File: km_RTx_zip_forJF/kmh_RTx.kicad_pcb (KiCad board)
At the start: 2 copper layers, 50 x 40 mm, 33 parts, among them IC1 ADP7118AUJZ-3.3-R7, J1 DE9_Receptacle, J3 Conn_Coaxial, J4 M80-5420442, T1 ETC4-1-2TR, U1 AD4PS-1+, U2 BD80FD0WHFP-TR, X1 3QHTF53-17.734-OE, X2 ASE-25.000MHZ-L-C-T, X3 3QHTF53-35.430-OE, X4 ASE-50.000MHZ-L-C-T

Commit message: C:\Users\khernandez\KiCad\KiCad-Project
Preliminary Part Placement
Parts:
- removed J1: DE9_Receptacle, Connector_Dsub:DSUB-9_Female_Horizontal_P2.77x2.84mm_EdgePinOffset9.40mm
- removed J3: Conn_Coaxial, Connector_Coaxial:SMA_Amphenol_132291_Vertical
- removed J4: M80-5420442, Connector:M80-5420442
- added H10: 2111-2-00-44-00-00-07-0, Turrets:2111200440000070, F.Cu at (94.0, 42.0)
- added H11: 2111-2-00-44-00-00-07-0, Turrets:2111200440000070, F.Cu at (94.0, 45.0)
- added H12: 2111-2-00-44-00-00-07-0, Turrets:2111200440000070, F.Cu at (94.0, 48.0)
- added H13: 2111-2-00-44-00-00-07-0, Turrets:2111200440000070, F.Cu at (94.0, 51.0)
- added H14: 2111-2-00-44-00-00-07-0, Turrets:2111200440000070, F.Cu at (129.5, 35.5)
- added H15: 2111-2-00-44-00-00-07-0, Turrets:2111200440000070, F.Cu at (129.5, 38.5)
- added H16: 2111-2-00-44-00-00-07-0, Turrets:2111200440000070, F.Cu at (129.5, 50.0)
- added H5: 2111-2-00-44-00-00-07-0, Turrets:2111200440000070, F.Cu at (90.5, 40.0)
- added H6: 2111-2-00-44-00-00-07-0, Turrets:2111200440000070, F.Cu at (90.5, 43.0)
- added H7: 2111-2-00-44-00-00-07-0, Turrets:2111200440000070, F.Cu at (90.5, 46.0)
- added H8: 2111-2-00-44-00-00-07-0, Turrets:2111200440000070, F.Cu at (90.5, 49.0)
- added H9: 2111-2-00-44-00-00-07-0, Turrets:2111200440000070, F.Cu at (90.5, 52.0)
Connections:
- R3 pad 2: Net-(J4-Pad3) -> unconnected-(R3-Pad2)

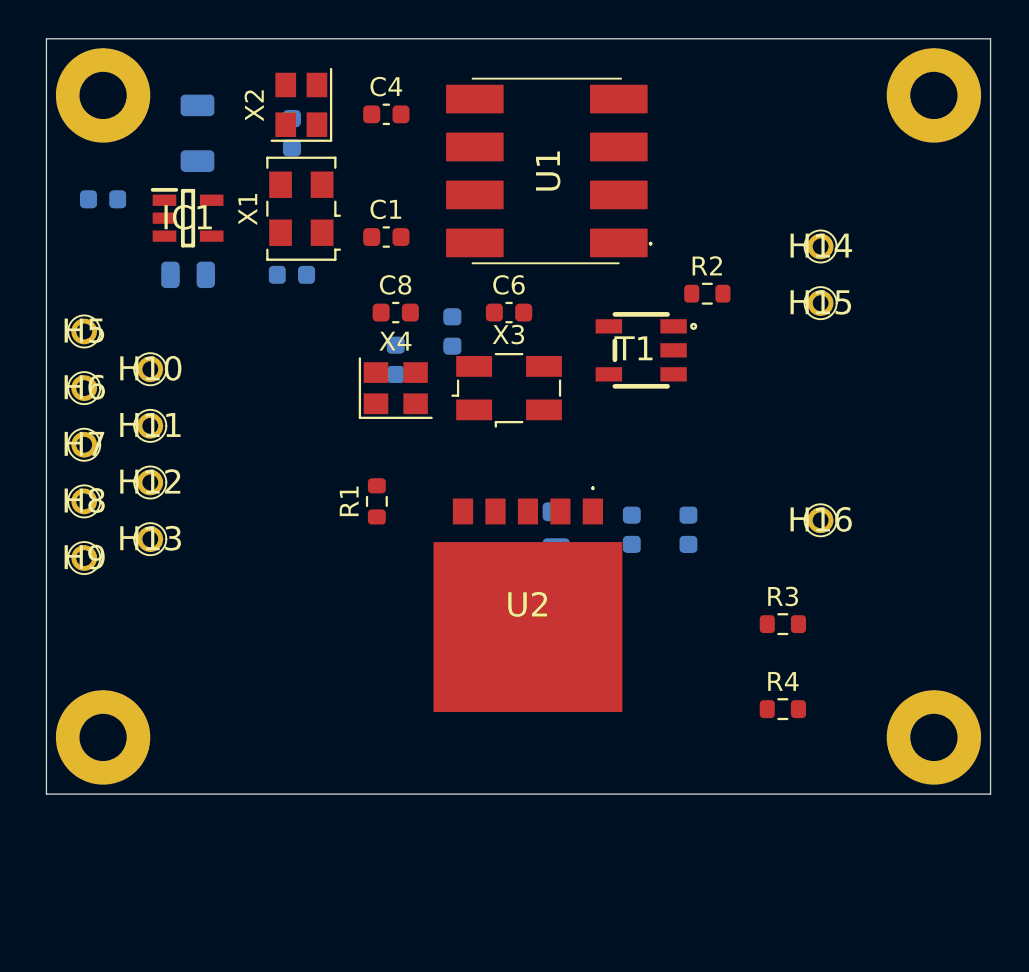
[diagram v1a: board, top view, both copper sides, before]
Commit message: Changed the voltage regulator to a chunky SOT23 package
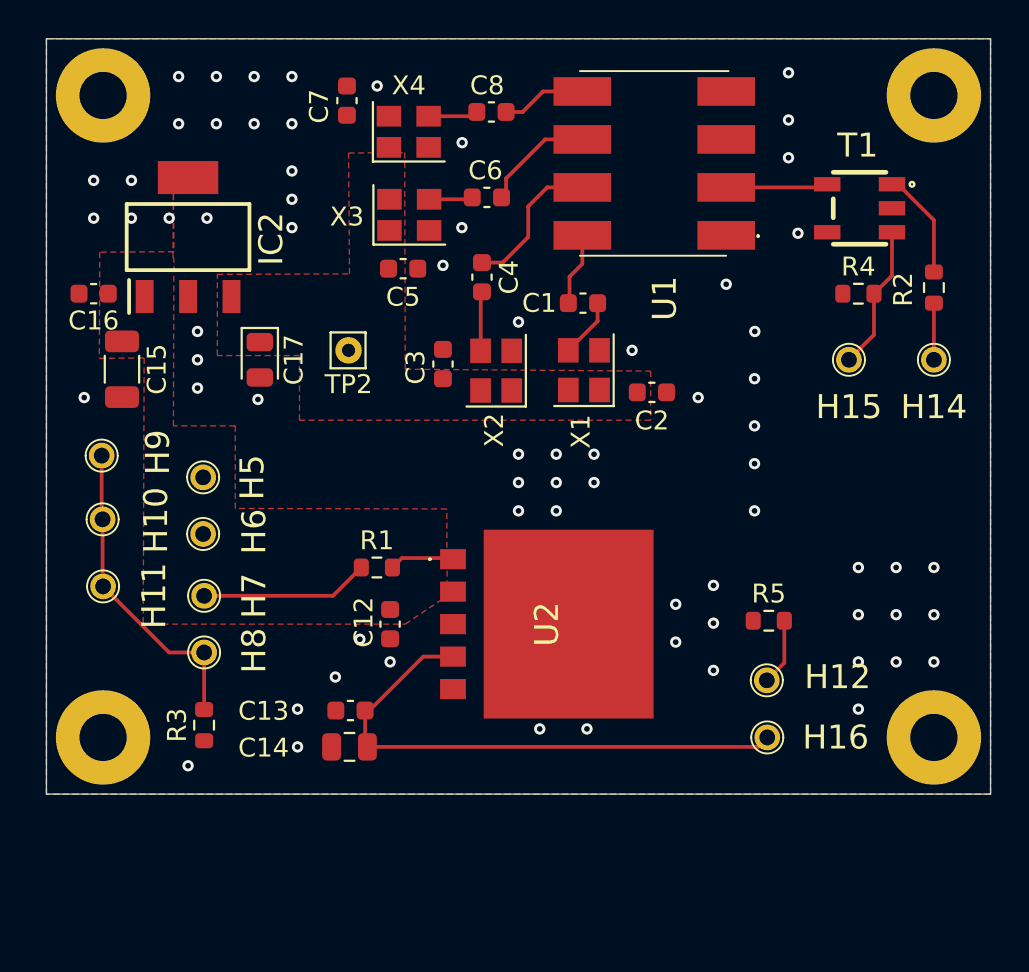
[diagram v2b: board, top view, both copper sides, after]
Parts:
- removed C10: 2.2uF, Diode_SMD:D_0805_2012Metric
- removed C11: 0.1uF, Capacitor_SMD:C_0603_1608Metric
- removed C9: 4.7uF, Capacitor_SMD:C_1206_3216Metric
- removed H13: 2111-2-00-44-00-00-07-0, Turrets:2111200440000070
- removed IC1: ADP7118AUJZ-3.3-R7, Package_SO:SOT95P280X100-5N
- added C15: 4.7uF, Capacitor_SMD:C_1206_3216Metric, F.Cu at (92.5, 42.0)
- added C16: 0.1uF, Capacitor_SMD:C_0603_1608Metric, F.Cu at (91.0, 38.0)
- added C17: 2.2uF, Diode_SMD:D_0805_2012Metric, F.Cu at (99.8, 41.5)
- added IC2: UA78M33QDCYRG4Q1, LDOs:SOT230P700X180-4N, F.Cu at (96.0, 35.0)
- added R5: 100M, Resistor_SMD:R_0603_1608Metric, F.Cu at (126.8, 55.3)
- added TP2: 3.3V, Connector_Pin:Pin_D0.7mm_L6.5mm_W1.8mm_FlatFork, F.Cu at (104.5, 41.0)
- C12, C13, C14, C2, C3, C5, C7: moved to F.Cu
- U2: footprint Lib:BD80FD0WHFPTR -> LDOs:BD80FD0WHFPTR
- X1: footprint Oscillator:Oscillator_SMD_TXC_7C-4Pin_5.0x3.2mm -> Oscillator:Oscillator_SMD_Abracon_ASE-4Pin_3.2x2.5mm
- X3: footprint Crystal:Crystal_SMD_EuroQuartz_MJ-4Pin_5.0x3.2mm -> Oscillator:Oscillator_SMD_Abracon_ASE-4Pin_3.2x2.5mm
- moved H12 34.3 mm to (126.7, 58.5)
- moved R3 31.1 mm to (96.8, 60.9), turned to 90 degrees
- moved R4 22.4 mm to (131.5, 38.0)
- moved C13 20.3 mm to (104.6, 60.1), turned to 180 degrees
- moved C2 20.1 mm to (120.6, 43.2)
- moved X2 17.5 mm to (112.3, 42.1)
- moved X1 17.2 mm to (117.0, 42.0)
- moved C14 15.9 mm to (104.5, 62.0), turned to 180 degrees
- moved C3 14.6 mm to (109.5, 41.7), turned to 90 degrees
- moved C7 14.0 mm to (104.4, 27.8), turned to 90 degrees
- moved T1 13.8 mm to (131.6, 33.5)
- moved C12 13.7 mm to (106.7, 55.5)
- moved X4 13.6 mm to (107.7, 29.4)
- moved R2 12.0 mm to (135.5, 37.7), turned to -90 degrees
- moved H16 11.8 mm to (126.7, 61.5)
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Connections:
- H10 pad 1: unconnected-(H10-Pad1) -> Net-(H10-Pad1)
- H11 pad 1: unconnected-(H11-Pad1) -> Net-(H10-Pad1)
- H12 pad 1: unconnected-(H12-Pad1) -> Net-(H12-Pad1)
- H5 pad 1: unconnected-(H5-Pad1) -> +15V
- H6 pad 1: unconnected-(H6-Pad1) -> +15V
- H7 pad 1: unconnected-(H7-Pad1) -> ReleaseAntenna
- H8 pad 1: unconnected-(H8-Pad1) -> Net-(H10-Pad1)
- H9 pad 1: unconnected-(H9-Pad1) -> Net-(H10-Pad1)
- R3 pad 2: unconnected-(R3-Pad2) -> Net-(H10-Pad1)
- U2 pad 4: Net-(J2-Pin_1) -> Net-(U2-VO)
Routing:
- net Net-(U2-VO): track 0.00 -> 29.2 mm
- net Net-(H10-Pad1): track 0.00 -> 16.8 mm
- net ReleaseAntenna: track 0.00 -> 8.95 mm
- net Net-(U1-PORT_2): track 0.00 -> 8.17 mm
- net GNDPWR: track 0.00 -> 7.70 mm
- net Net-(U1-PORT_3): track 0.00 -> 5.80 mm
- net Net-(R2-Pad1): track 0.00 -> 5.75 mm
- net Net-(U1-SUM_PORT): track 0.00 -> 5.42 mm
- net Net-(U1-PORT_4): track 0.00 -> 4.49 mm
- net Net-(U1-PORT_1): track 0.00 -> 3.90 mm
- net Net-(H12-Pad1): track 0.00 -> 3.54 mm
- net Net-(U2-CTL): track 0.00 -> 3.44 mm
- net Net-(X2-OUT): track 0.00 -> 3.16 mm
- net Net-(X1-OUT): track 0.00 -> 3.14 mm
- net Net-(H14-Pad1): track 0.00 -> 3.00 mm
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- added copper zone on F.Cu, net +15V
- added copper zone on F.Cu, net +3.3V
- added copper zone on B.Cu, net GND
- added copper zone on F.Cu, net GND

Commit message: More routing done
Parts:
- removed H12: 2111-2-00-44-00-00-07-0, Turrets:2111200440000070
- added R10: 0, Resistor_SMD:R_0603_1608Metric, F.Cu at (130.2, 37.2)
- added R11: 0, Resistor_SMD:R_0603_1608Metric, F.Cu at (133.5, 45.5)
- added R12: 100M, Resistor_SMD:R_0603_1608Metric, F.Cu at (130.5, 56.8)
- added R6: 8.16k, Resistor_SMD:R_0603_1608Metric, F.Cu at (108.7, 61.5)
- added R7: 68k, Resistor_SMD:R_0603_1608Metric, F.Cu at (108.0, 59.0)
- added R8: 0, Resistor_SMD:R_0603_1608Metric, F.Cu at (129.8, 41.0)
- added R9: 0, Resistor_SMD:R_0603_1608Metric, F.Cu at (136.8, 41.0)
- added T2: ETC4-1-2TR, RF_Componets:ETC4_1_2TR, F.Cu at (133.5, 40.7)
- added TP1: 14.3625_MHz, Test_Points:5000, F.Cu at (121.2, 39.0)
- added TP3: 20.8875_MHz, Test_Points:5000, F.Cu at (113.8, 35.8)
- added TP4: 29.5625 MHz, Test_Points:5000, F.Cu at (113.8, 32.0)
- added TP5: 41.8125 MHz, Test_Points:5000, F.Cu at (113.8, 27.8)
- added TP6: SUM_OUT, Test_Points:5000, F.Cu at (130.2, 29.2)
- added TP7: GROUND, Test_Points:5000, F.Cu at (126.2, 51.2)
- C12: footprint Capacitor_SMD:C_0603_1608Metric -> Capacitor_SMD:C_1206_3216Metric
- C13: value 1uF -> 2.2uF; footprint Capacitor_SMD:C_0603_1608Metric -> Capacitor_SMD:C_1206_3216Metric
- J1: renamed from H16; value 2111-2-00-44-00-00-07-0 -> 0022232031; footprint Turrets:2111200440000070 -> Connector_PinHeader_2.54mm:PinHeader_1x03_P2.54mm_Vertical
- T1: footprint Transformer_SMD:E_SERIES_1 -> RF_Componets:ETC4_1_2TR
- U1: footprint RF:AD4PS1 -> RF_Componets:AD4PS1
- U2: value BD80FD0WHFP-TR -> BD00D0AWHFP-TR; footprint LDOs:BD80FD0WHFPTR -> LDOs:HRP5_ROM
- X1: value 3QHTF53-17.734-OE -> ASSFLP-R-C02; footprint Oscillator:Oscillator_SMD_Abracon_ASE-4Pin_3.2x2.5mm -> Crystal:Crystal_SMD_Abracon_ABM3B-4Pin_5.0x3.2mm
- X2: value ASE-25.000MHZ-L-C-T -> ASSFLP-R-C02; footprint Oscillator:Oscillator_SMD_Abracon_ASE-4Pin_3.2x2.5mm -> Crystal:Crystal_SMD_Abracon_ABM3B-4Pin_5.0x3.2mm
- X3: value 3QHTF53-35.430-OE -> ASSFLP-R-C02; footprint Oscillator:Oscillator_SMD_Abracon_ASE-4Pin_3.2x2.5mm -> Crystal:Crystal_SMD_Abracon_ABM3B-4Pin_5.0x3.2mm
- X4: value ASE-50.000MHZ-L-C-T -> ASSFLP-R-C02; footprint Oscillator:Oscillator_SMD_Abracon_ASE-4Pin_3.2x2.5mm -> Crystal:Crystal_SMD_Abracon_ABM3B-4Pin_5.0x3.2mm
- moved R4 8.27 mm to (131.0, 46.2)
- moved H14 8.00 mm to (135.5, 49.5)
- moved H15 8.00 mm to (131.0, 49.5)
- moved R2 7.83 mm to (135.5, 45.5)
- moved C14 6.17 mm to (106.0, 56.0), turned to 90 degrees
- moved J1 5.28 mm to (126.5, 56.2)
- moved R5 5.25 mm to (130.5, 59.0), turned to 180 degrees
- moved C12 4.01 mm to (107.0, 51.5), turned to 90 degrees
- moved C7 3.95 mm to (100.5, 27.3)
- moved C13 3.74 mm to (103.5, 56.5), turned to 90 degrees
- moved C3 3.05 mm to (107.8, 44.2)
- moved X4 2.97 mm to (104.8, 29.0)
- moved X3 2.97 mm to (104.8, 33.8)
- moved C2 2.81 mm to (121.0, 46.0)
- moved R1 2.76 mm to (103.2, 52.2)
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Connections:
- C13 pad 1: Net-(U2-VO) -> Net-(J1-Pin_3)
- C14 pad 1: Net-(U2-VO) -> Net-(J1-Pin_3)
- J1 pad 1: Net-(U2-VO) -> Net-(J1-Pin_1)
- R5 pad 2: Net-(H12-Pad1) -> Net-(J1-Pin_2)
- T1 pad 1: Net-(R2-Pad1) -> Net-(R9-Pad1)
- T1 pad 2: unconnected-(T1-Pad2) -> Net-(R10-Pad1)
- T1 pad 3: GNDPWR -> Net-(R8-Pad1)
- U2 pad 4: Net-(U2-VO) -> Net-(J1-Pin_3)
- U2 pad 5: unconnected-(U2-N.C.-Pad5) -> Net-(U2-ADJ)
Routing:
- net Net-(J1-Pin_3): track 0.00 -> 36.6 mm
- net Net-(U2-VO): track 29.2 -> 0.00 mm
- net GNDPWR: track 7.70 -> 18.3 mm
- net Net-(R9-Pad1): track 0.00 -> 10.1 mm
- net Net-(R8-Pad1): track 0.00 -> 7.64 mm
- net Net-(U1-PORT_1): track 3.90 -> 11.3 mm
- net Net-(U2-ADJ): track 0.00 -> 5.19 mm
- net Net-(R10-Pad1): track 0.00 -> 4.86 mm
- net Net-(H12-Pad1): track 3.54 -> 0.00 mm
- net Net-(J1-Pin_2): track 0.00 -> 3.51 mm
- net Net-(J1-Pin_1): track 0.00 -> 3.39 mm
- net Net-(U2-CTL): track 3.44 -> 6.74 mm
- net Net-(U1-PORT_2): track 8.17 -> 11.2 mm
- net Net-(U1-PORT_4): track 4.49 -> 7.36 mm
- net Net-(U1-PORT_3): track 5.80 -> 8.46 mm
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
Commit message: C:\Users\khernandez\KiCad\KiCad-Projects# Please enter the commit message for your changes. Lines starting
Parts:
- removed H15: 2111-2-00-44-00-00-07-0, Turrets:2111200440000070
- removed R11: 0, Resistor_SMD:R_0603_1608Metric
- J1: value 0022232031 -> Conn_01x06_Pin; footprint Connector_PinHeader_2.54mm:PinHeader_1x03_P2.54mm_Vertical -> Connectors_kmh:22232061
- R12, R3, R4, R5: value 100M -> 10M
- R8: value 0 -> 10K
- T1, T2: value ETC4-1-2TR -> ADT16-1T+; footprint RF_Componets:ETC4_1_2TR -> RF_Componets:ADT161T
- moved R3 37.0 mm to (133.0, 53.0), turned to 180 degrees
- moved R8 28.1 mm to (103.1, 49.8), turned to 180 degrees
- moved TP7 11.9 mm to (136.5, 57.2)
- moved R9 10.7 mm to (127.0, 45.5)
- moved R10 9.30 mm to (124.8, 44.8), turned to -90 degrees
- moved R2 8.40 mm to (130.5, 52.2)
- moved R4 8.33 mm to (136.5, 52.5), turned to 90 degrees
- moved H14 8.00 mm to (133.5, 57.2)
- moved J1 6.75 mm to (124.8, 62.7), turned to 90 degrees
- moved T2 5.04 mm to (133.3, 45.8), turned to 180 degrees
- moved T1 2.82 mm to (133.5, 35.5), turned to -90 degrees
- moved TP6 2.02 mm to (130.0, 27.2)
- moved R1 0.79 mm to (103.0, 51.5)
- moved R12 0.56 mm to (130.2, 56.2)
- moved R5 0.56 mm to (130.2, 58.5)
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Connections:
- C13 pad 1: Net-(J1-Pin_3) -> Net-(J1-Pin_1)
- C14 pad 1: Net-(J1-Pin_3) -> Net-(J1-Pin_1)
- H10 pad 1: Net-(H10-Pad1) -> GND
- H11 pad 1: Net-(H10-Pad1) -> GND
- H8 pad 1: Net-(H10-Pad1) -> GND
- H9 pad 1: Net-(H10-Pad1) -> GND
- J1 pad 2: Net-(J1-Pin_2) -> GND
- J1 pad 3: Net-(J1-Pin_3) -> GND
- R10 pad 1: Net-(R10-Pad1) -> Net-(T1-SA)
- R12 pad 2: Net-(J1-Pin_1) -> Net-(J1-Pin_6)
- R2 pad 1: Net-(R2-Pad1) -> Net-(T2-SB)
- R3 pad 2: Net-(H10-Pad1) -> Net-(H14-Pad1)
- R5 pad 2: Net-(J1-Pin_2) -> Net-(J1-Pin_5)
- R7 pad 1: Net-(J1-Pin_3) -> Net-(J1-Pin_1)
- R8 pad 1: Net-(R8-Pad1) -> Net-(U2-CTL)
- R8 pad 2: GNDPWR -> GND
- R9 pad 1: Net-(R9-Pad1) -> Net-(T1-SB)
- R9 pad 2: Net-(R2-Pad1) -> Net-(T2-SB)
- T1 pad 1: Net-(R9-Pad1) -> Net-(T1-AA)
- T1 pad 2: Net-(R10-Pad1) -> (no net)
- T1 pad 3: Net-(R8-Pad1) -> GND
- T1 pad 4: GND -> Net-(T1-SB)
- T1 pad 5: Net-(U1-SUM_PORT) -> GNDPWR
- T2 pad 1: Net-(R2-Pad1) -> Net-(T1-SB)
- T2 pad 2: Net-(R11-Pad1) -> (no net)
- T2 pad 3: GNDPWR -> Net-(T1-SA)
- T2 pad 4: Net-(R8-Pad1) -> Net-(T2-SB)
- T2 pad 5: Net-(R9-Pad1) -> unconnected-(T2-SC-Pad5)
- TP6 pad 1: Net-(U1-SUM_PORT) -> Net-(T1-AA)
- U1 pad 2: Net-(U1-SUM_PORT) -> Net-(T1-AA)
- U2 pad 4: Net-(J1-Pin_3) -> Net-(J1-Pin_1)
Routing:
- net Net-(J1-Pin_3): track 36.6 -> 0.00 mm
- net Net-(J1-Pin_1): track 3.39 -> 34.0 mm
- net Net-(T1-SA): track 0.00 -> 18.8 mm
- net Net-(H10-Pad1): track 16.8 -> 0.00 mm
- net Net-(T1-SB): track 0.00 -> 15.0 mm
- net Net-(T1-AA): track 0.00 -> 13.9 mm
- net GND: track 0.00 -> 13.8 mm, vias 79 -> 74
- net GNDPWR: track 18.3 -> 30.8 mm
- net Net-(R9-Pad1): track 10.1 -> 0.00 mm
- net Net-(T2-SB): track 0.00 -> 8.85 mm
- net Net-(J1-Pin_6): track 0.00 -> 8.14 mm
- net Net-(J1-Pin_5): track 0.00 -> 7.85 mm
- net Net-(R8-Pad1): track 7.64 -> 0.00 mm
- net Net-(U1-SUM_PORT): track 7.01 -> 0.00 mm
- net Net-(R10-Pad1): track 4.86 -> 0.00 mm
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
